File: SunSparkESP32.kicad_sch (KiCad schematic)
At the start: 54 parts, among them J1 Conn_01x02_Pin, J2 USB_C_Receptacle_USB2.0, J3 Conn_01x03_Pin, J4 Conn_01x15_Pin, J5 Conn_01x03_Pin, J6 Conn_01x15_Pin, J7 Conn_01x01_Pin, J8 Conn_01x01_Pin, Q1 IRLML6244TRPBF, Q2 IRLML6244TRPBF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

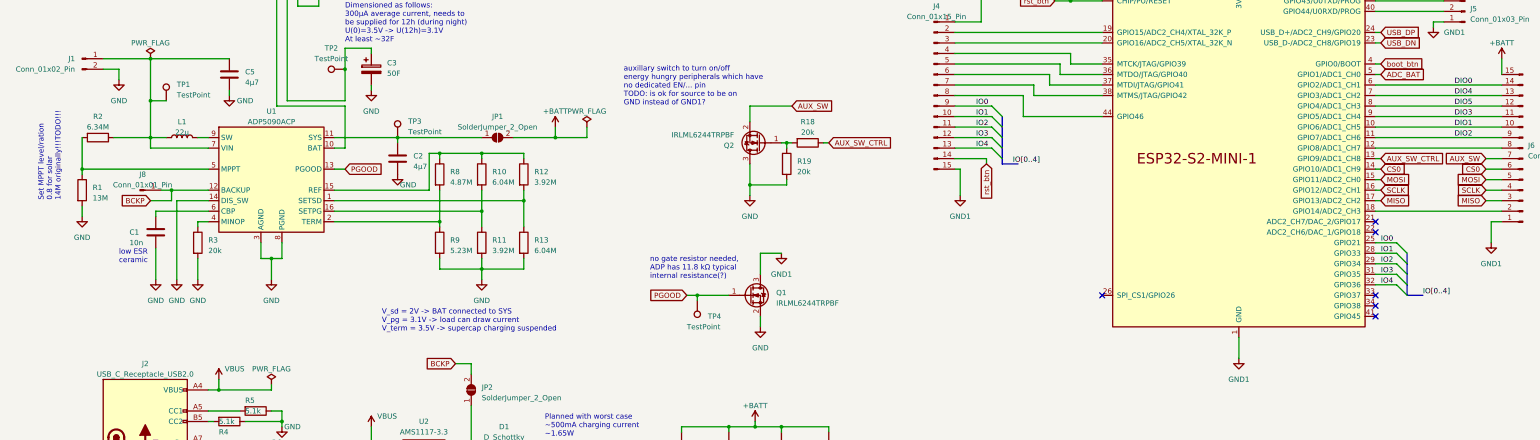
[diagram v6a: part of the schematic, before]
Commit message: Various fixes due to V2 testing -GPIO46 now not routed to external pin header -Corrected some silk -Cleaned up schematic
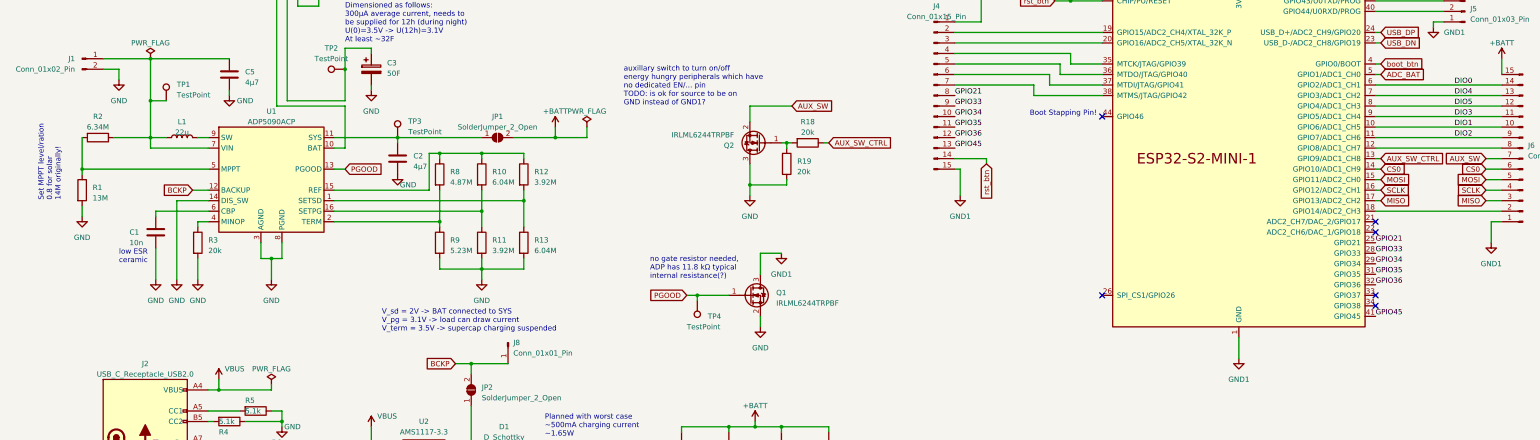
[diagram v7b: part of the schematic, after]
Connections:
- net GPIO45: now reaches U3.41 (GPIO45)
- net GPIO45: now also J4.13 (Pin_13)
- net at U3.44 (GPIO46): no longer J4.8 (Pin_8)
- net IO0 renamed GPIO21
- net GPIO21: now also J4.8 (Pin_8); no longer J4.9 (Pin_9)
- net IO1 renamed GPIO33
- net GPIO33: now also J4.9 (Pin_9); no longer J4.10 (Pin_10)
- net IO2 renamed GPIO34
- net GPIO34: now also J4.10 (Pin_10); no longer J4.11 (Pin_11)
- net IO3 renamed GPIO35
- net GPIO35: now also J4.11 (Pin_11); no longer J4.12 (Pin_12)
- net IO4 renamed GPIO36
- net GPIO36: now also J4.12 (Pin_12); no longer J4.13 (Pin_13)
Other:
- note added: "Boot Stapping Pin!"
- note added: "Set MPPT level/ration 0.8 for solar 14M originally!"
- note removed: "Set MPPT level/ration 0.8 for solar 14M originally!!!TODO!!!"
- moved on the sheet: J8

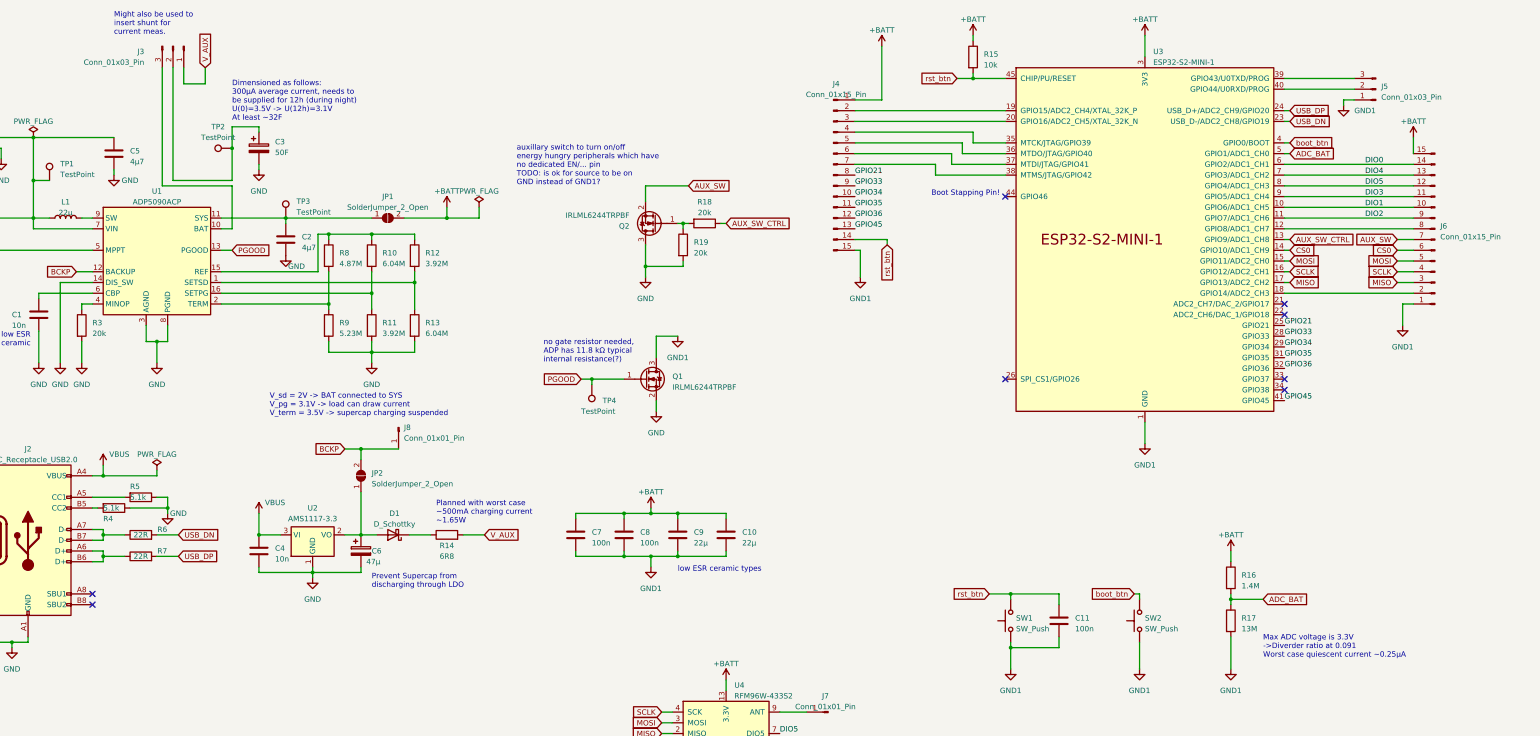
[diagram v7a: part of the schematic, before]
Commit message: Removed some debugging connectors -Directly connected backup supply -Removed series connector to supercap
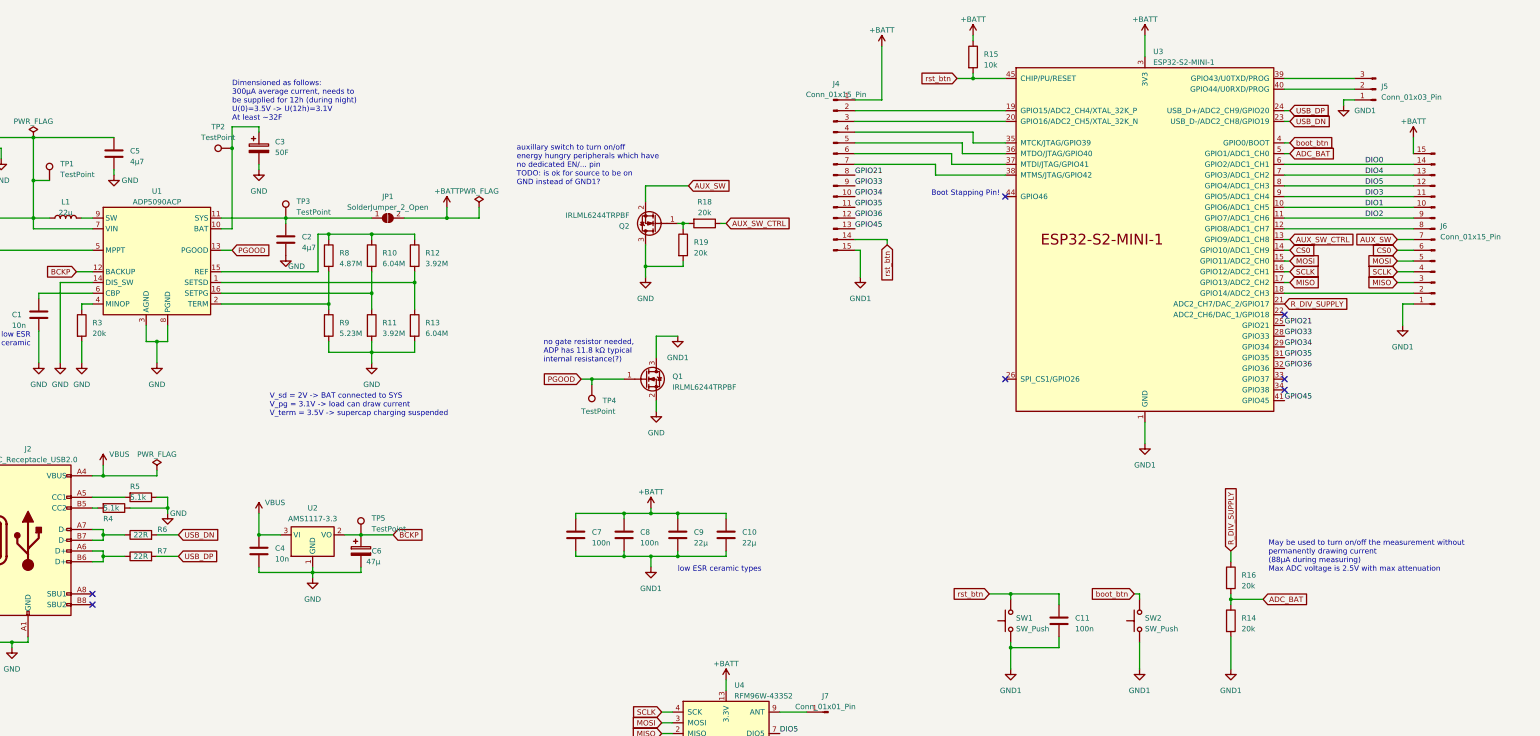
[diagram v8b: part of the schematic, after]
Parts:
- removed D1: D_Schottky, Diode_SMD:D_SOD-323, symbol Device:D_Schottky
- removed J3: Conn_01x03_Pin, Connector_PinSocket_2.54mm:PinSocket_1x03_P2.54mm_Vertical, symbol Connector:Conn_01x03_Pin
- removed J8: Conn_01x01_Pin, TestPoint:TestPoint_THTPad_D1.5mm_Drill0.7mm, symbol Connector:Conn_01x01_Pin
- removed JP2: SolderJumper_2_Open, Jumper:SolderJumper-2_P1.3mm_Open_RoundedPad1.0x1.5mm, symbol Jumper:SolderJumper_2_Open
- removed R17: 13M, Resistor_SMD:R_0805_2012Metric_Pad1.20x1.40mm_HandSolder, symbol Device:R
- added TP5: TestPoint, TestPoint:TestPoint_Pad_D1.0mm, symbol Connector:TestPoint
- R14: value 6R8 -> 20k; footprint Resistor_SMD:R_0612_1632Metric -> Resistor_SMD:R_0805_2012Metric_Pad1.20x1.40mm_HandSolder
- R16: value 1.4M -> 20k
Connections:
- net V_AUX is gone; now on net GND1: R14.2
- net +BATT: no longer R16.1
- net ADC_BAT: now also R14.1
- net BCKP: now also C6.1, U2.2 (VO), TP5.1
- net at C3.1, TP2.1: now also U1.10 (BAT)
- net R_DIV_SUPPLY: now reaches U3.21 (ADC2_CH7/DAC_2/GPIO17)
- net R_DIV_SUPPLY: now also R16.1
- no-connect marks 8 -> 7
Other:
- note added: "May be used to turn on/off the measurement without permanently drawing current (88µA during measuring) Max ADC voltage is 2.5V with max attenuation"
- note removed: "Max ADC voltage is 3.3V ->Diverder ratio at 0.091 Worst case quiescent current ~0.25µA"
- note removed: "Might also be used to insert shunt for current meas."
- note removed: "Planned with worst case ~500mA charging current ~1.65W"
- note removed: "Prevent Supercap from discharging through LDO"
